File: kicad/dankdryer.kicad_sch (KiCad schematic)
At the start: 23 parts, among them J11 testpin, J13 barreljack, J9 UART, SW2 bootmode, U1 TPS62132, U6 ESP32-C6-MINI-1U

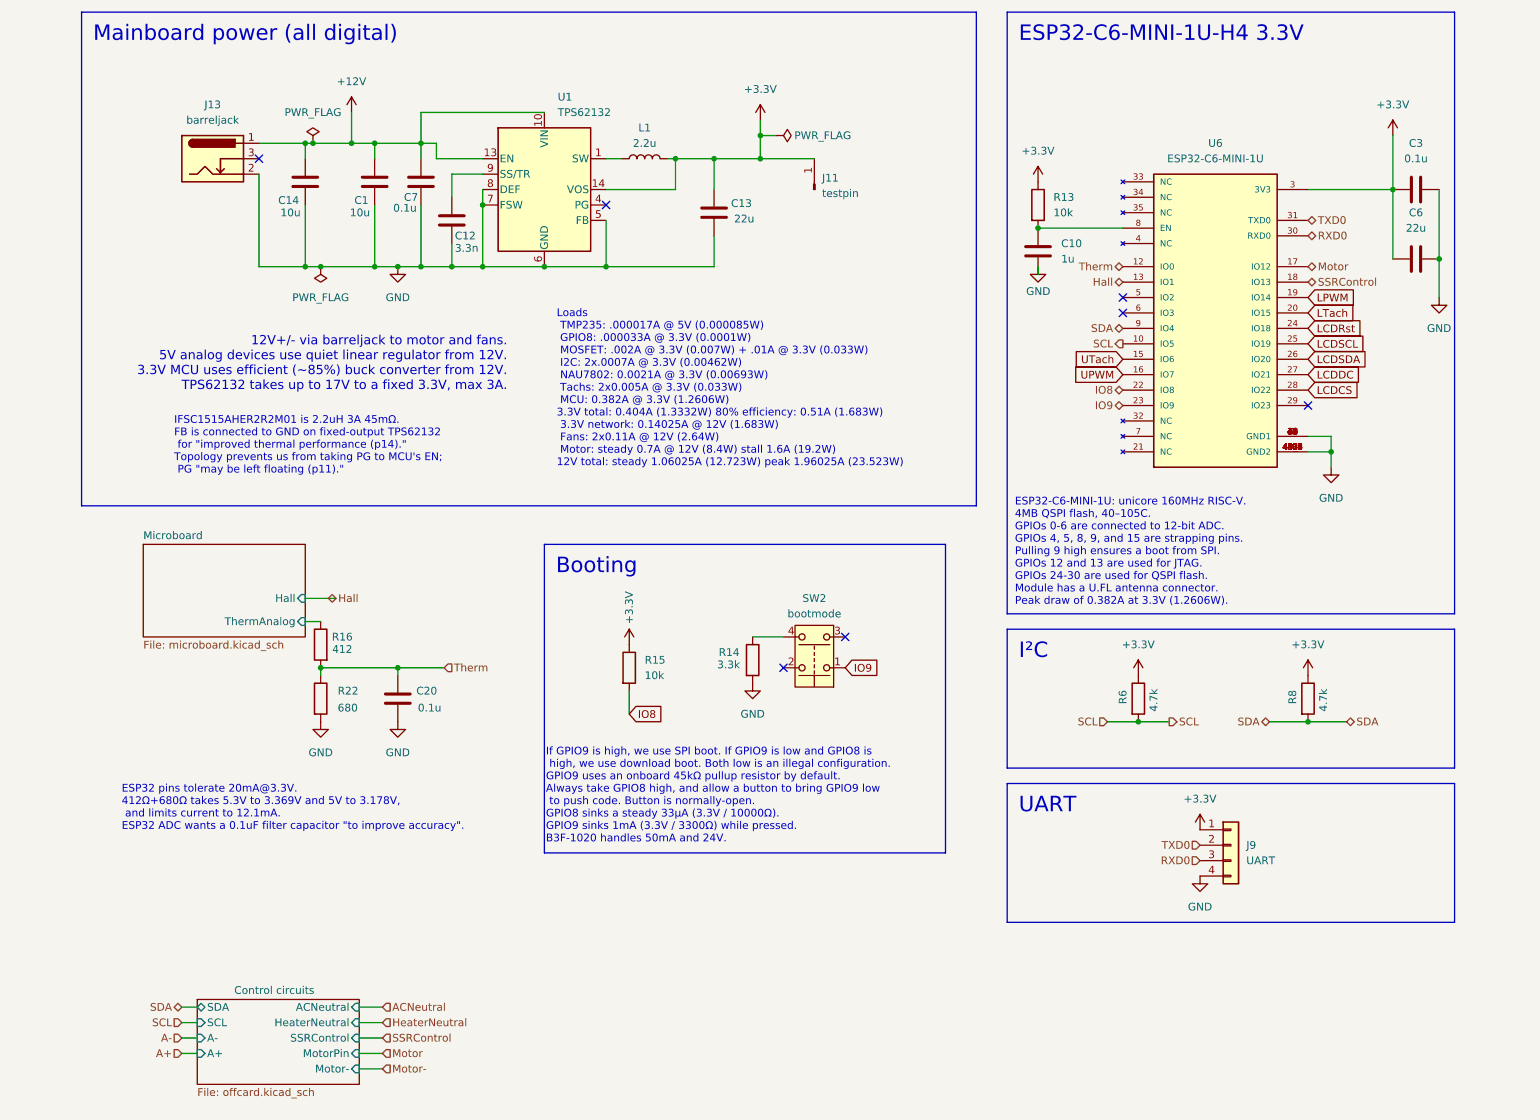
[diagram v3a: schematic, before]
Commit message: update footprint for tps62132
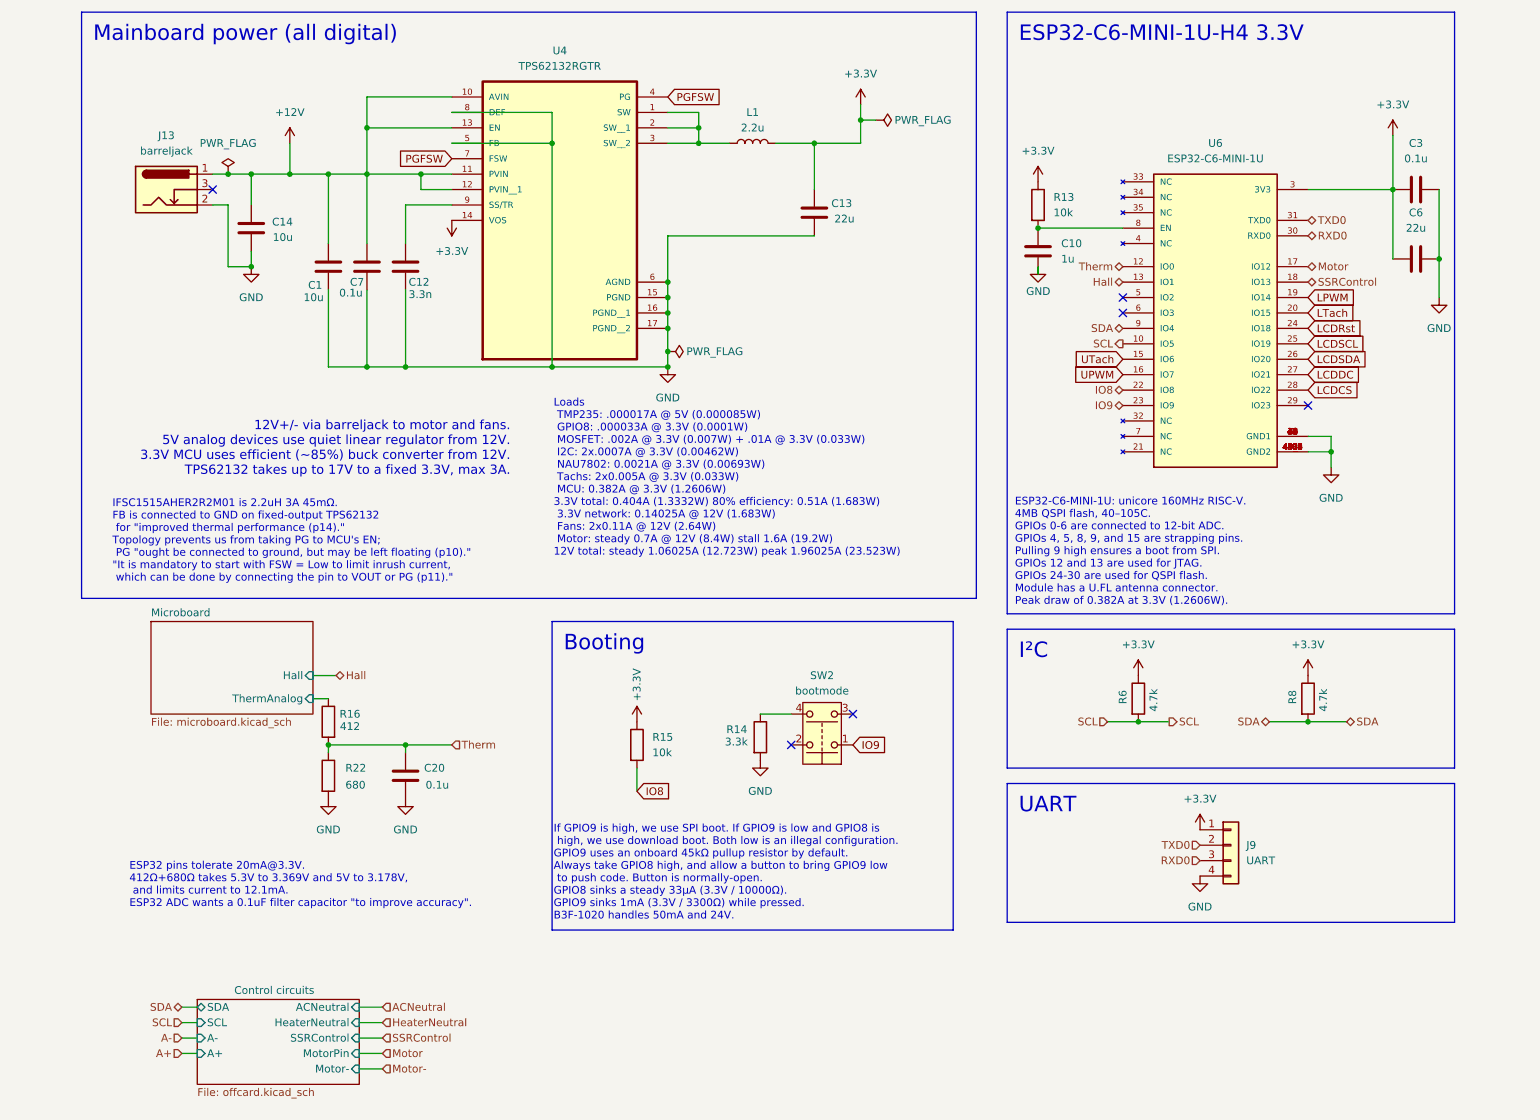
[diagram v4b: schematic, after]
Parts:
- removed J11: testpin, Connector_PinHeader_1.00mm:PinHeader_1x01_P1.00mm_Vertical, symbol Connector:Conn_01x01_Pin
- removed U1: TPS62132, dank:TPS62132, symbol dank:TPS62132
- added U4: TPS62132RGTR, dank:TPS62132RGTR, symbol dank:TPS62132RGTR
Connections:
- net +12V: now also U4.10 (AVIN), U4.11 (PVIN), U4.12 (PVIN__1), U4.13 (EN)
- net +3.3V: now also U4.14 (VOS)
- net GND: now also U4.15 (PGND), U4.16 (PGND__1), U4.17 (PGND__2), U4.5 (FB), U4.6 (AGND), U4.8 (DEF)
- net at L1.1: now also U4.1 (SW), U4.2 (SW__1), U4.3 (SW__2)
- net at C12.1: now also U4.9 (SS/TR)
- new net PGFSW: U4.4 (PG), U4.7 (FSW)
- no-connect marks 7 -> 6
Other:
- note added: "IFSC1515AHER2R2M01 is 2.2uH 3A 45mΩ. FB is connected to GND on fixed-output TPS62132 for "improved thermal performance (p14)." Topology prevents us from taking PG to MCU's EN; PG "ought be connected to ground, but may be left floating (p10)." "It is mandatory to start with FSW = Low to limit inrush current, which can be done by connecting the pin to VOUT or PG (p11).""
- note removed: "IFSC1515AHER2R2M01 is 2.2uH 3A 45mΩ. FB is connected to GND on fixed-output TPS62132 for "improved thermal performance (p14)." Topology prevents us from taking PG to MCU's EN; PG "may be left floating (p11).""
- moved on the sheet: C1, C12, C13, C14, C20, C7, J13, L1, R14, R15, R16, R22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

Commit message: [miniboard] throughholes need [5, -5] separation #99
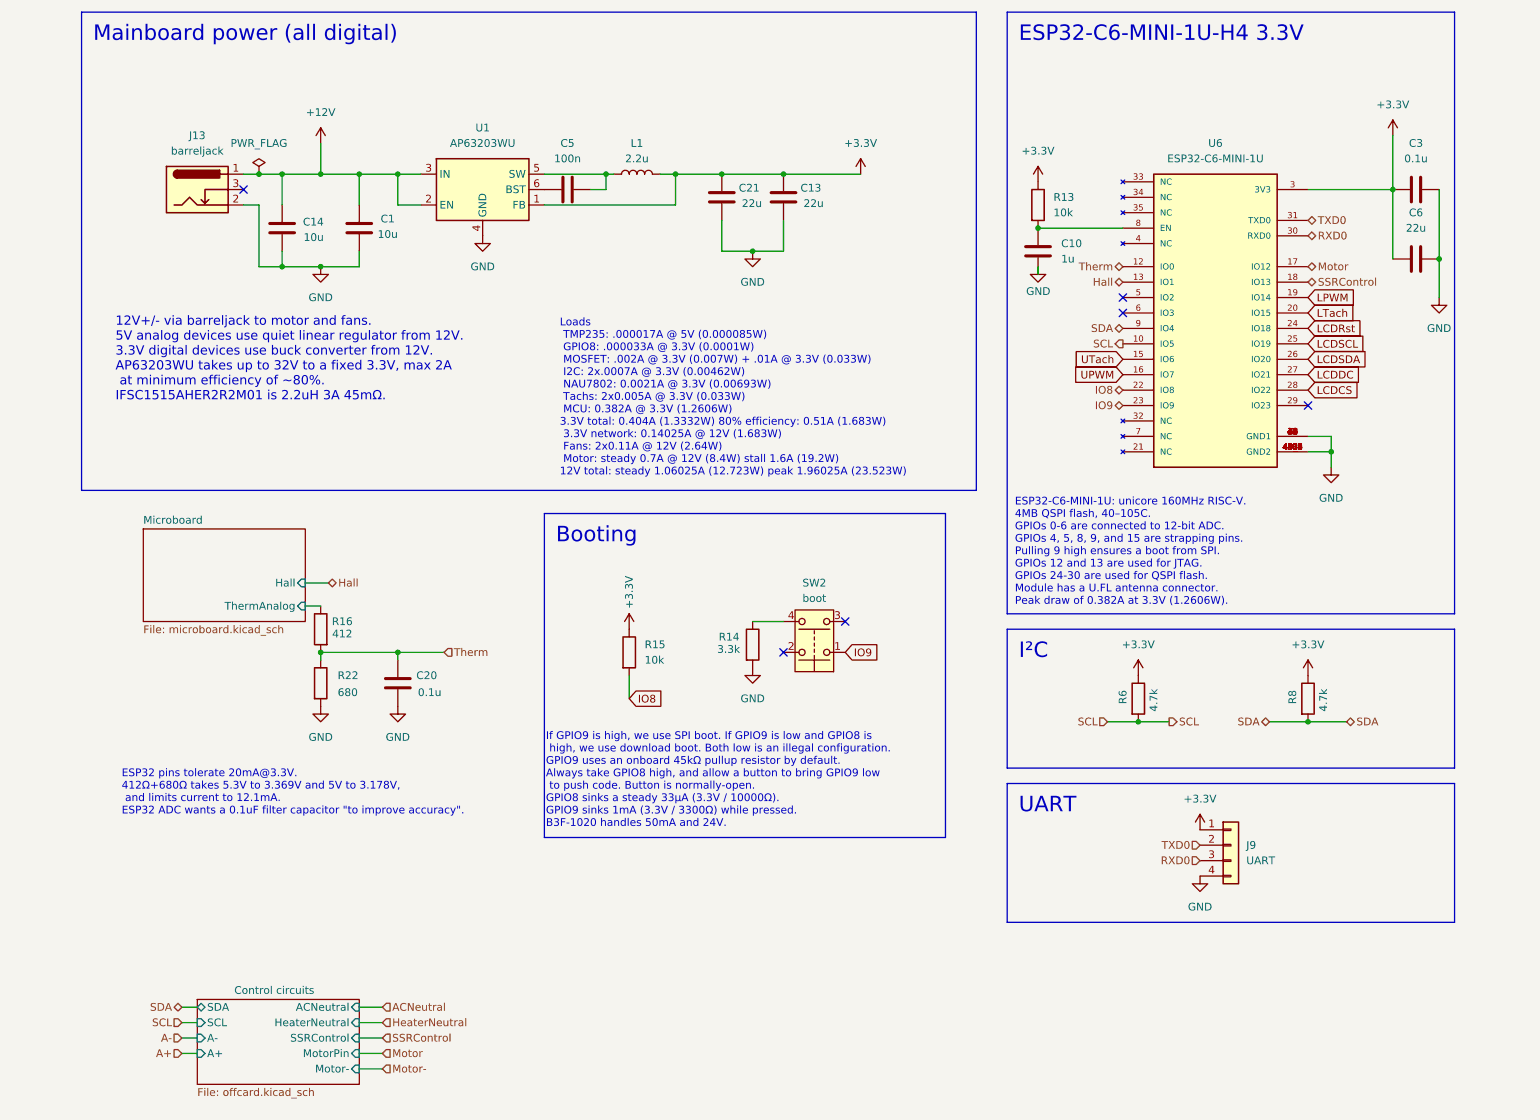
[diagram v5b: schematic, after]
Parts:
- removed C12: 3.3n, Capacitor_SMD:C_1206_3216Metric_Pad1.33x1.80mm_HandSolder, symbol Device:C
- removed C7: 0.1u, Capacitor_SMD:C_1206_3216Metric_Pad1.33x1.80mm_HandSolder, symbol Device:C
- removed U4: TPS62132RGTR, dank:TPS62132RGTR, symbol dank:TPS62132RGTR
- added C21: 22u, Capacitor_SMD:C_0805_2012Metric_Pad1.18x1.45mm_HandSolder, symbol Device:C
- added C5: 100n, Capacitor_SMD:C_0805_2012Metric_Pad1.18x1.45mm_HandSolder, symbol Device:C
- added U1: AP63203WU, Package_TO_SOT_SMD:TSOT-23-6, symbol Regulator_Switching:AP63203WU
- C1, C13, C14: footprint Capacitor_SMD:C_1206_3216Metric_Pad1.33x1.80mm_HandSolder -> Capacitor_SMD:C_0805_2012Metric_Pad1.18x1.45mm_HandSolder
- R14, R15: footprint Resistor_SMD:R_1206_3216Metric_Pad1.30x1.75mm_HandSolder -> Resistor_SMD:R_0805_2012Metric_Pad1.20x1.40mm_HandSolder
- SW2: value bootmode -> boot
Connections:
- net +12V: now also U1.2 (EN), U1.3 (IN)
- net +3.3V: now also C21.1, U1.1 (FB)
- net GND: now also C21.2, U1.4 (GND)
- net at L1.1: now also C5.2, U1.5 (SW)
- new net: C5.1, U1.6 (BST)
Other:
- note added: "12V+/- via barreljack to motor and fans. 5V analog devices use quiet linear regulator from 12V. 3.3V digital devices use buck converter from 12V. AP63203WU takes up to 32V to a fixed 3.3V, max 2A at minimum efficiency of ~80%. IFSC1515AHER2R2M01 is 2.2uH 3A 45mΩ."
- note removed: "12V+/- via barreljack to motor and fans. 5V analog devices use quiet linear regulator from 12V. 3.3V MCU uses efficient (~85%) buck converter from 12V. TPS62132 takes up to 17V to a fixed 3.3V, max 3A."
- note removed: "IFSC1515AHER2R2M01 is 2.2uH 3A 45mΩ. FB is connected to GND on fixed-output TPS62132 for "improved thermal performance (p14)." Topology prevents us from taking PG to MCU's EN; PG "ought be connected to ground, but may be left floating (p10)." "It is mandatory to start with FSW = Low to limit inrush current, which can be done by connecting the pin to VOUT or PG (p11).""
- moved on the sheet: C1, C13, C14, C20, J13, L1, R14, R15, R16, R22, SW2
